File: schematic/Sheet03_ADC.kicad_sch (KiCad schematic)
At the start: 15 parts, among them U1 ADC12DJ5200-SP

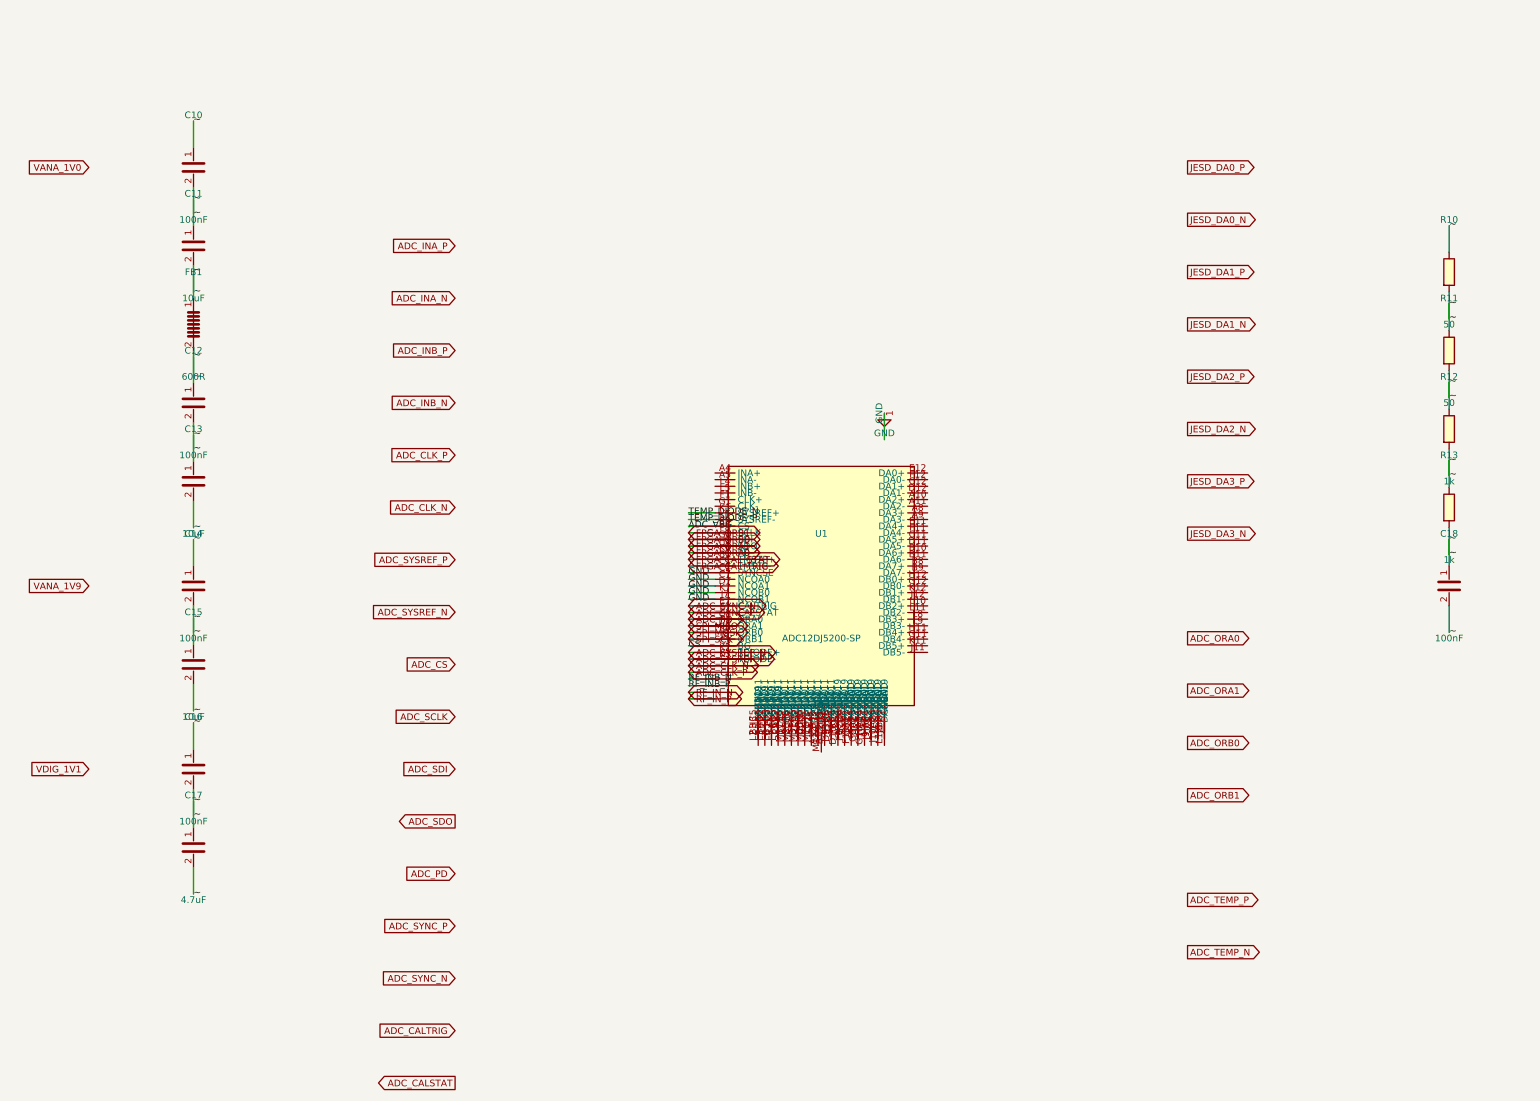
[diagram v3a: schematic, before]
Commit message: Fix KiCad schematic wiring: Y-inversion bug + all 891 pins connected
- Fixed critical Y-axis inversion bug: KiCad inverts Y when placing
  symbols (lib Y + schematic Y = abs Y is WRONG; correct: abs Y = sym Y - lib Y)
- This caused ALL wires to connect to wrong pins (e.g., CS label connected
  to BG pin instead of CS pin)
- Verified with netlist: 0 unconnected nets, all pin functions correct
- Fixed wire direction for angle 90/270 (swapped due to Y-inversion)
- 891 pin connections across 15 sheets, all 17 sheets export without errors
- Netlist verification: CS→E8, BG→C3, INA+→A4, CLK+→F1, JESD pairs correct

Co-Authored-By: opencode <noreply@opencode.ai>
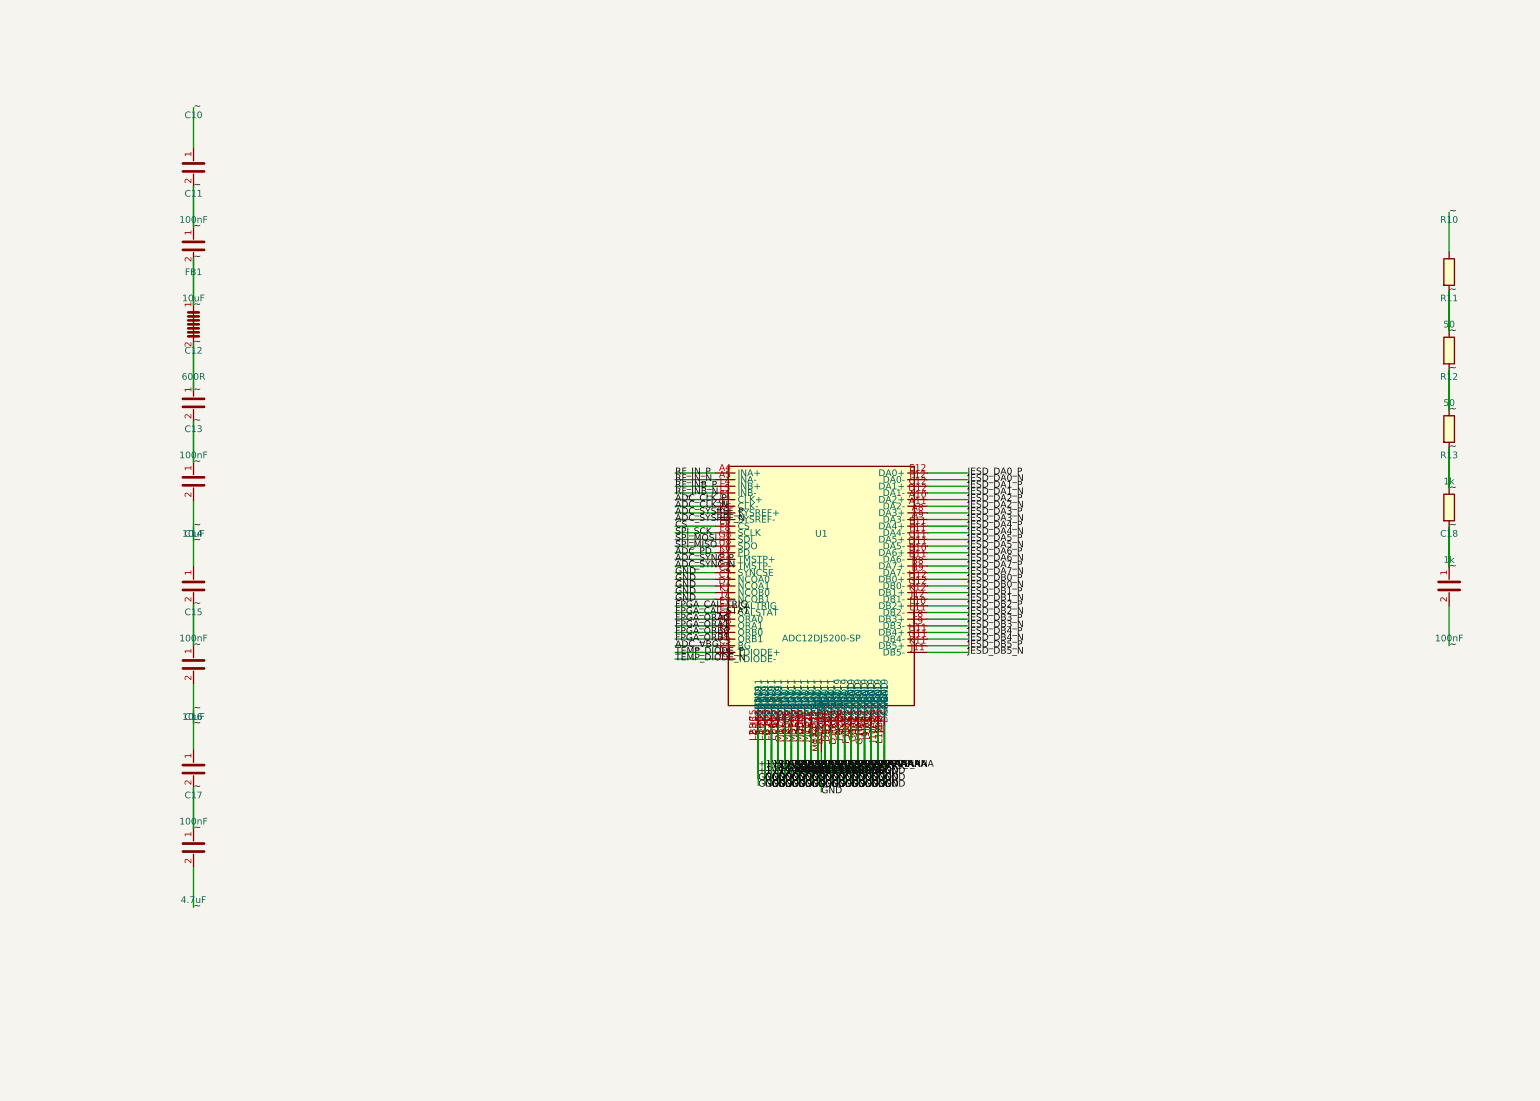
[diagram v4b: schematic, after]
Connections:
- net GND is gone; now on net +1V0_ANA: U1.C2 (SYNCSE), U1.C7 (NCOA0), U1.D7 (NCOA1), U1.J7 (NCOB1), U1.K7 (NCOB0)
- net ADC_CLK_N: now also U1.G1 (CLK-)
- net ADC_CLK_P: now also U1.F1 (CLK+)
- net ADC_PD: now also U1.K6 (PD); no longer U1.C8 (ORA0)
- net ADC_SYNC_N: now also U1.C1 (TMSTP-); no longer U1.E7 (CALTRIG)
- net ADC_SYNC_P: now also U1.B1 (TMSTP+); no longer U1.F7 (CALSTAT)
- net ADC_SYSREF_N: now also U1.L1 (SYSREF-); no longer U1.K2 (TDIODE+)
- net ADC_SYSREF_P: now also U1.K1 (SYSREF+); no longer U1.K3 (TDIODE-)
- net ADC_VBG: now also U1.C3 (BG); no longer U1.E8 (CS)
- net CS: now also U1.E8 (CS); no longer U1.C3 (BG)
- net FPGA_CAL_STAT: now also U1.F7 (CALSTAT); no longer U1.B1 (TMSTP+)
- net FPGA_CAL_TRIG: now also U1.E7 (CALTRIG); no longer U1.C1 (TMSTP-)
- net FPGA_ORA0: now also U1.C8 (ORA0); no longer U1.K6 (PD)
- net FPGA_ORA1: now also U1.D8 (ORA1); no longer U1.H8 (SDO)
- net FPGA_ORB0: now also U1.K8 (ORB0); no longer U1.G8 (SDI)
- net FPGA_ORB1: now also U1.J8 (ORB1); no longer U1.F8 (SCLK)
- net JESD_DA0_N: now also U1.F12 (DA0-)
- net JESD_DA0_P: now also U1.E12 (DA0+)
- net JESD_DA1_N: now also U1.D12 (DA1-)
- net JESD_DA1_P: now also U1.C12 (DA1+)
- net JESD_DA2_N: now also U1.A11 (DA2-)
- net JESD_DA2_P: now also U1.A10 (DA2+)
- net JESD_DA3_N: now also U1.A9 (DA3-)
- net JESD_DA3_P: now also U1.A8 (DA3+)
- net RF_INB_N: now also U1.L5 (INB-)
- net RF_INB_P: now also U1.L4 (INB+)
- net RF_IN_N: now also U1.A5 (INA-)
- net RF_IN_P: now also U1.A4 (INA+)
- net SPI_MISO: now also U1.H8 (SDO); no longer U1.D8 (ORA1)
- net SPI_MOSI: now also U1.G8 (SDI); no longer U1.K8 (ORB0)
- net SPI_SCK: now also U1.F8 (SCLK); no longer U1.J8 (ORB1)
- net TEMP_DIODE_N: now also U1.K3 (TDIODE-); no longer U1.K1 (SYSREF+)
- net TEMP_DIODE_P: now also U1.K2 (TDIODE+); no longer U1.L1 (SYSREF-)
- net +1V0_ANA: now reaches U1.A1 (AGND)
- net +1V0_ANA: now also U1.A12 (DGND), U1.A2 (AGND), U1.A3 (AGND), U1.A6 (AGND), U1.A7 (AGND), U1.B12 (DGND), U1.B2 (AGND), U1.B3 (AGND), U1.B4 (AGND), U1.B5 (AGND), U1.B6 (AGND), U1.B7 (AGND), U1.C10 (VD11), U1.C4 (VA19), U1.C5 (VA11), U1.C6 (AGND), U1.C9 (VD11), U1.D1 (AGND), U1.D10 (DGND), U1.D2 (VA11), U1.D3 (VA11), U1.D4 (VA19), U1.D5 (VA11), U1.D6 (AGND), U1.D9 (DGND), U1.E1 (AGND), U1.E10 (VD11), U1.E2 (VA19), U1.E3 (VA19), U1.E4 (VA19), U1.E5 (VA11), U1.E6 (AGND), U1.E9 (VD11), U1.F10 (DGND), U1.F2 (AGND), U1.F3 (AGND), U1.F4 (VA19), U1.F5 (VA11), U1.F6 (AGND), U1.F9 (DGND), U1.G10 (DGND), U1.G2 (AGND), U1.G3 (AGND), U1.G4 (VA19), U1.G5 (VA11), U1.G6 (AGND), U1.G7 (VD11), U1.G9 (DGND), U1.H1 (AGND), U1.H10 (VD11), U1.H2 (VA19), U1.H3 (VA19), U1.H4 (VA19), U1.H5 (VA11), U1.H6 (AGND), U1.H7 (VD11), U1.H9 (VD11), U1.J1 (AGND), U1.J10 (DGND), U1.J2 (VA11), U1.J3 (VA11), U1.J4 (VA19), U1.J5 (VA11), U1.J6 (AGND), U1.J9 (DGND), U1.K10 (VD11), U1.K4 (VA19), U1.K5 (VA11), U1.K9 (VD11), U1.L12 (DGND), U1.L2 (AGND), U1.L3 (AGND), U1.L6 (AGND), U1.L7 (AGND), U1.M1 (AGND), U1.M12 (DGND), U1.M2 (AGND), U1.M3 (AGND), U1.M6 (AGND), U1.M7 (AGND)
- net JESD_DA6_P: now reaches U1.B10 (DA6+)
- net JESD_DA6_N: now reaches U1.B11 (DA6-)
- net JESD_DA7_P: now reaches U1.B8 (DA7+)
- net JESD_DA7_N: now reaches U1.B9 (DA7-)
- net JESD_DA5_P: now reaches U1.C11 (DA5+)
- net JESD_DA5_N: now reaches U1.D11 (DA5-)
- net JESD_DA4_P: now reaches U1.E11 (DA4+)
- net JESD_DA4_N: now reaches U1.F11 (DA4-)
- net JESD_DB4_N: now reaches U1.G11 (DB4-)
- net JESD_DB0_N: now reaches U1.G12 (DB0-)
- net JESD_DB4_P: now reaches U1.H11 (DB4+)
- net JESD_DB0_P: now reaches U1.H12 (DB0+)
- net JESD_DB5_N: now reaches U1.J11 (DB5-)
- net JESD_DB1_N: now reaches U1.J12 (DB1-)
- net JESD_DB5_P: now reaches U1.K11 (DB5+)
- net JESD_DB1_P: now reaches U1.K12 (DB1+)
- net JESD_DB2_P: now reaches U1.L10 (DB2+)
- net JESD_DB2_N: now reaches U1.L11 (DB2-)
- net JESD_DB3_P: now reaches U1.L8 (DB3+)
- net JESD_DB3_N: now reaches U1.L9 (DB3-)

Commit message: fix: use horizontal wire stubs to prevent KiCad net merging
Root cause: vertical wires from stacked power pins (1.27mm spacing)
overlapped when wire length > pin spacing, causing KiCad to merge
all power nets into one. Also skip unnamed (~) passive component pins.

Changes:
- Always use horizontal LEFT stubs regardless of pin angle
- Skip pins with net_name '~' (capacitor/resistor unnamed pins)
- 557 pin connections across 13 sheets, all pass KiCad CLI

NOTE: power net separation still shows all power_in pins on one net
in kicad-cli netlist export - needs further investigation.
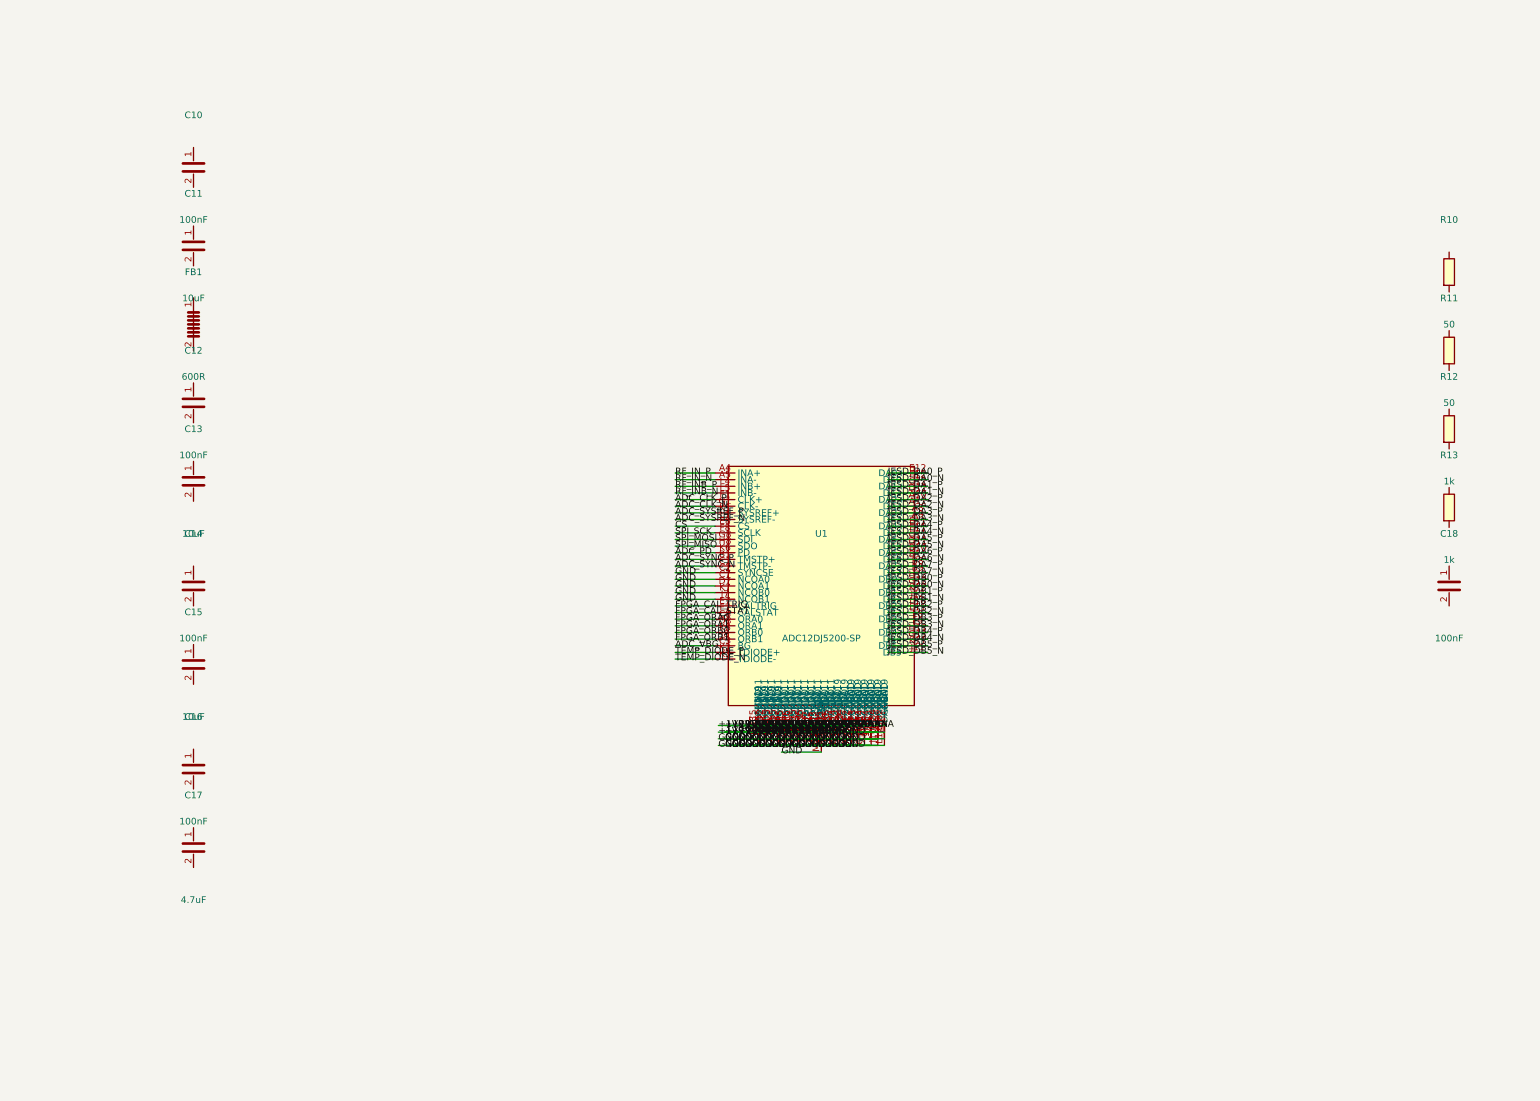
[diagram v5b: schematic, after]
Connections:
- removed net ~: C10.1, C10.2, C11.1, C11.2, C12.1, C12.2, C13.1, C13.2, C14.1, C14.2, C15.1, C15.2, C16.1, C16.2, C17.1, C17.2, C18.1, C18.2, FB1.1, FB1.2, R10.1, R10.2, R11.1, R11.2, R12.1, R12.2, R13.1, R13.2

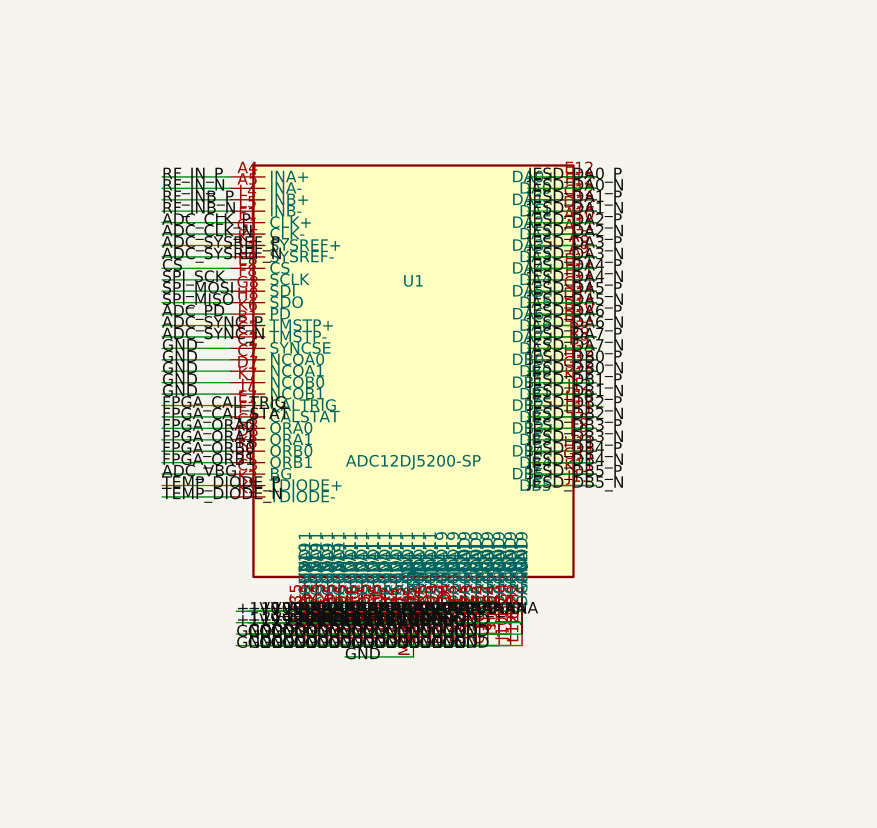
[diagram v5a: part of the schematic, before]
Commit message: fix: replace wire stubs with labels-only to prevent power net shorts
Labels placed directly at pin endpoints eliminate wire overlap that
caused BGA power pins (VA11, VA19, VD11, AGND, DGND) to merge into
a single net. Verified via netlist: GND=52, +1V0_ANA=12, +1V9_ANA=12,
+1V1_DIG=10 nodes (all correct per datasheet pin mapping).
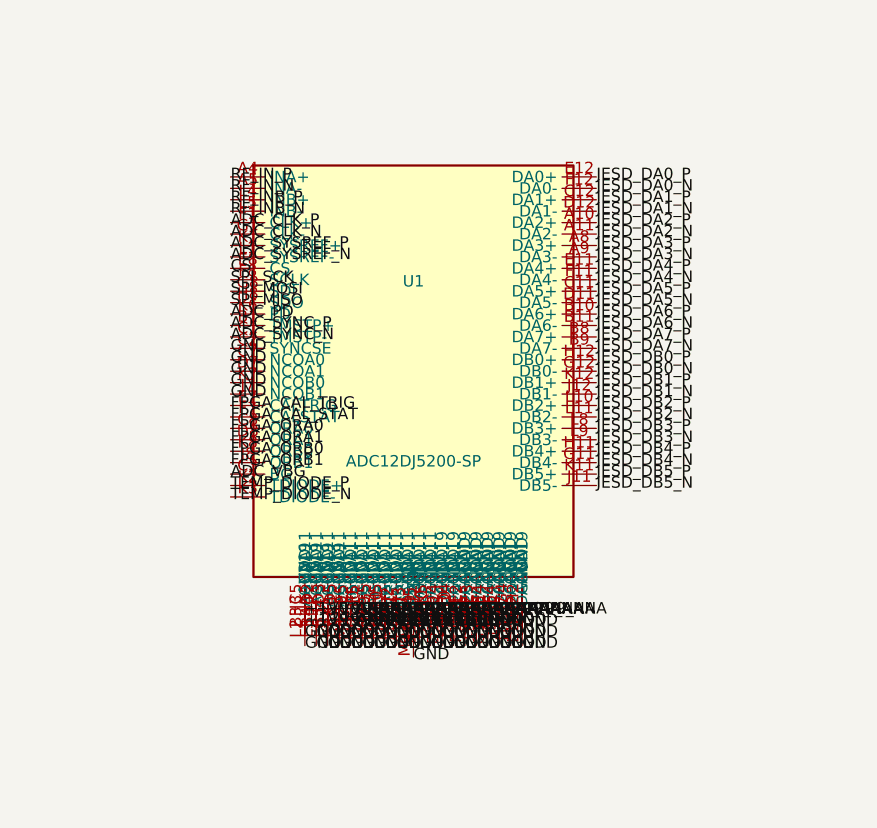
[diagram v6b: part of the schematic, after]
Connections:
- net +1V0_ANA: no longer U1.A1 (AGND), U1.A12 (DGND), U1.A2 (AGND), U1.A3 (AGND), U1.A6 (AGND), U1.A7 (AGND), U1.B12 (DGND), U1.B2 (AGND), U1.B3 (AGND), U1.B4 (AGND), U1.B5 (AGND), U1.B6 (AGND), U1.B7 (AGND), U1.C10 (VD11), U1.C2 (SYNCSE), U1.C4 (VA19), U1.C6 (AGND), U1.C7 (NCOA0), U1.C9 (VD11), U1.D1 (AGND), U1.D10 (DGND), U1.D4 (VA19), U1.D6 (AGND), U1.D7 (NCOA1), U1.D9 (DGND), U1.E1 (AGND), U1.E10 (VD11), U1.E2 (VA19), U1.E3 (VA19), U1.E4 (VA19), U1.E6 (AGND), U1.E9 (VD11), U1.F10 (DGND), U1.F2 (AGND), U1.F3 (AGND), U1.F4 (VA19), U1.F6 (AGND), U1.F9 (DGND), U1.G10 (DGND), U1.G2 (AGND), U1.G3 (AGND), U1.G4 (VA19), U1.G6 (AGND), U1.G7 (VD11), U1.G9 (DGND), U1.H1 (AGND), U1.H10 (VD11), U1.H2 (VA19), U1.H3 (VA19), U1.H4 (VA19), U1.H6 (AGND), U1.H7 (VD11), U1.H9 (VD11), U1.J1 (AGND), U1.J10 (DGND), U1.J4 (VA19), U1.J6 (AGND), U1.J7 (NCOB1), U1.J9 (DGND), U1.K10 (VD11), U1.K4 (VA19), U1.K7 (NCOB0), U1.K9 (VD11), U1.L12 (DGND), U1.L2 (AGND), U1.L3 (AGND), U1.L6 (AGND), U1.L7 (AGND), U1.M1 (AGND), U1.M12 (DGND), U1.M2 (AGND), U1.M3 (AGND), U1.M6 (AGND), U1.M7 (AGND)
- new net +1V1_DIG: U1.C10 (VD11), U1.C9 (VD11), U1.E10 (VD11), U1.E9 (VD11), U1.G7 (VD11), U1.H10 (VD11), U1.H7 (VD11), U1.H9 (VD11), U1.K10 (VD11), U1.K9 (VD11)
- new net +1V9_ANA: U1.C4 (VA19), U1.D4 (VA19), U1.E2 (VA19), U1.E3 (VA19), U1.E4 (VA19), U1.F4 (VA19), U1.G4 (VA19), U1.H2 (VA19), U1.H3 (VA19), U1.H4 (VA19), U1.J4 (VA19), U1.K4 (VA19)
- new net GND: U1.A1 (AGND), U1.A12 (DGND), U1.A2 (AGND), U1.A3 (AGND), U1.A6 (AGND), U1.A7 (AGND), U1.B12 (DGND), U1.B2 (AGND), U1.B3 (AGND), U1.B4 (AGND), U1.B5 (AGND), U1.B6 (AGND), U1.B7 (AGND), U1.C2 (SYNCSE), U1.C6 (AGND), U1.C7 (NCOA0), U1.D1 (AGND), U1.D10 (DGND), U1.D6 (AGND), U1.D7 (NCOA1), U1.D9 (DGND), U1.E1 (AGND), U1.E6 (AGND), U1.F10 (DGND), U1.F2 (AGND), U1.F3 (AGND), U1.F6 (AGND), U1.F9 (DGND), U1.G10 (DGND), U1.G2 (AGND), U1.G3 (AGND), U1.G6 (AGND), U1.G9 (DGND), U1.H1 (AGND), U1.H6 (AGND), U1.J1 (AGND), U1.J10 (DGND), U1.J6 (AGND), U1.J7 (NCOB1), U1.J9 (DGND), U1.K7 (NCOB0), U1.L12 (DGND), U1.L2 (AGND), U1.L3 (AGND), U1.L6 (AGND), U1.L7 (AGND), U1.M1 (AGND), U1.M12 (DGND), U1.M2 (AGND), U1.M3 (AGND), U1.M6 (AGND), U1.M7 (AGND)

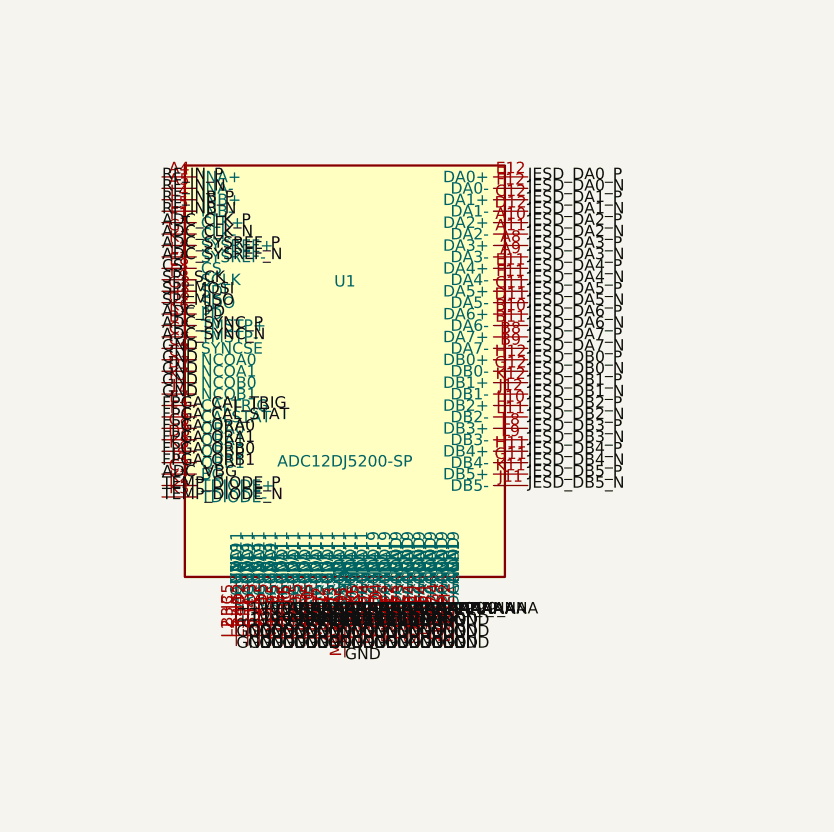
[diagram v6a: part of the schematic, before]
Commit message: fix: isolate ISL70003ASEH buck pins, fix LMX_SYNC collision, NC pins, connector pin names
- ISL70003ASEH pins now use ref prefix (U6_LX1 vs U7_LX1) to prevent shorts
- Buck SYNC pins separated from LMX_SYNC (power sync ≠ PLL sync)
- NC pins properly skipped (unconnected)
- Connector PIN_1..PIN_6 use ref prefix (J1_PIN_1 vs J2_PIN_1)
- Fixed annotation warnings in Sheet13 (C_dev→C125, R_dev→R74, U_TPS7H→U14)
- Regenerated all PDFs and SVGs
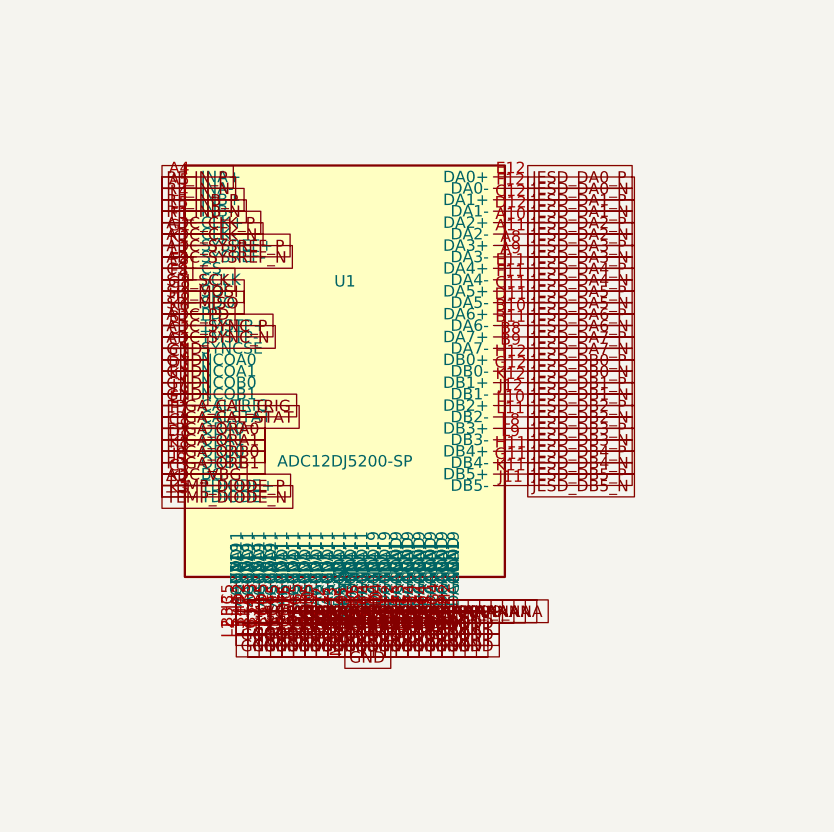
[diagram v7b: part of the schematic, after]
